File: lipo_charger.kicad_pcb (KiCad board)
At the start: 2 copper layers, 42 x 51 mm, 13 parts, among them P1 CONN_01X02, P2 CONN_01X02, Q1 BC557, Q2 BC547, U1 MCP73831

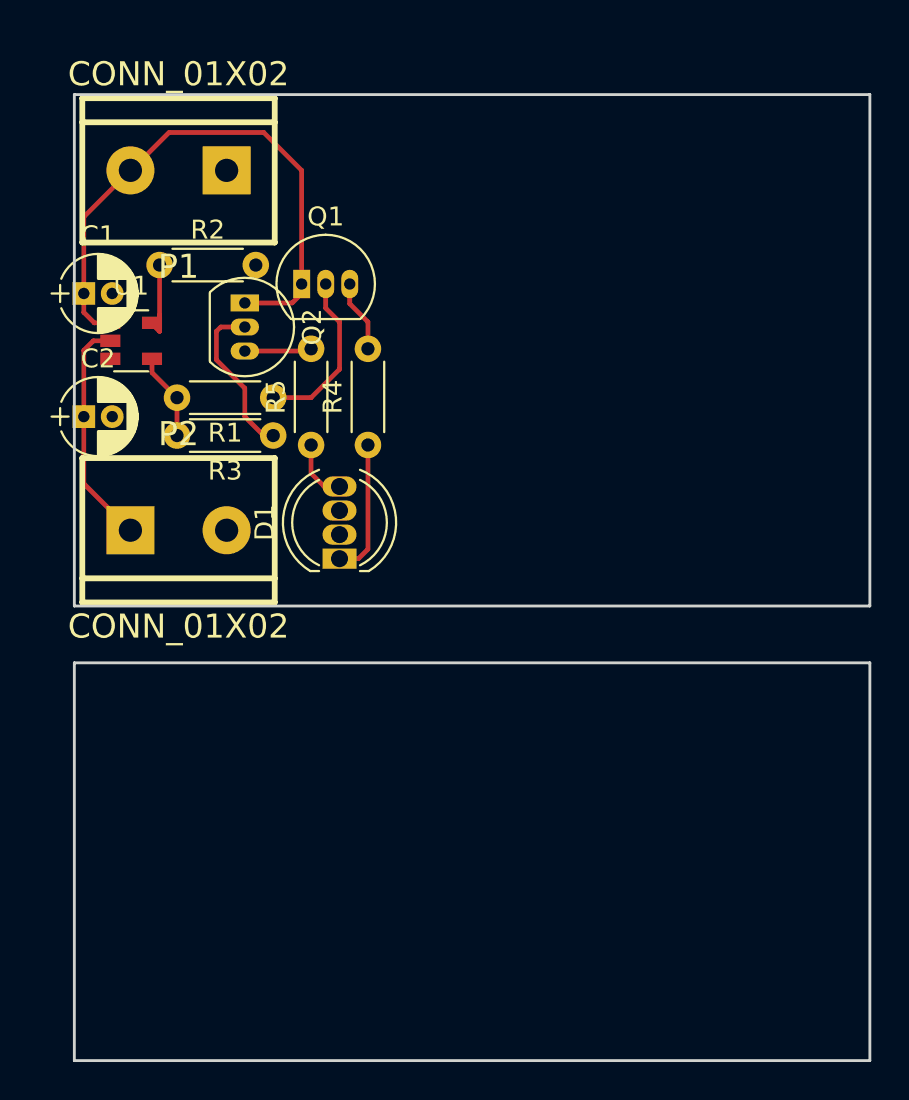
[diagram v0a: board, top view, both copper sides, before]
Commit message: 3x lipo charger with tracks
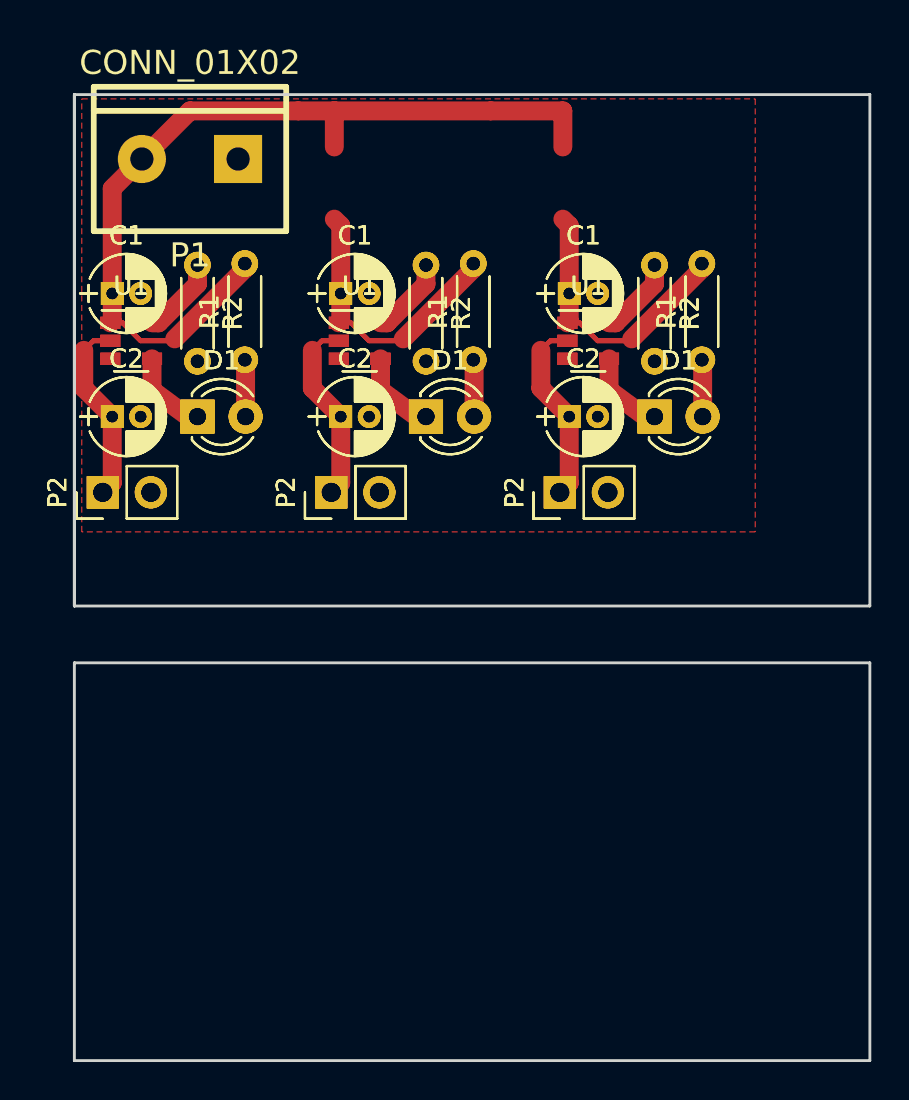
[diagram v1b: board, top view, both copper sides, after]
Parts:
- removed the D1 at (86.0, 46.5)
- removed the P2 at (77.5, 45.0)
- removed Q1: BC557, TO_SOT_Packages_THT:TO-92_Inline_Narrow_Oval
- removed Q2: BC547, TO_SOT_Packages_THT:TO-92_Inline_Narrow_Oval
- removed R3: 2k, Resistors_ThroughHole:R_Axial_DIN0204_L3.6mm_D1.6mm_P5.08mm_Horizontal
- removed R4, R5: 220R, Resistors_ThroughHole:R_Axial_DIN0204_L3.6mm_D1.6mm_P5.08mm_Horizontal
- added C1 (x2): 4.7uF, Capacitors_THT:CP_Radial_D4.0mm_P1.50mm, F.Cu at (98.1, 32.5)
- added C1 (x2): 4.7uF, Capacitors_THT:CP_Radial_D4.0mm_P1.50mm, F.Cu at (86.1, 32.5)
- added C1: 4.7uF, Capacitors_THT:CP_Radial_D4.0mm_P1.50mm, F.Cu at (74.0, 32.5)
- added C2 (x2): 4.7uF, Capacitors_THT:CP_Radial_D4.0mm_P1.50mm, F.Cu at (98.1, 39.0)
- added C2 (x2): 4.7uF, Capacitors_THT:CP_Radial_D4.0mm_P1.50mm, F.Cu at (86.1, 39.0)
- added C2: 4.7uF, Capacitors_THT:CP_Radial_D4.0mm_P1.50mm, F.Cu at (74.0, 39.0)
- added D1 (x2): LED, LEDs:LED_D3.0mm, F.Cu at (102.6, 39.0)
- added D1 (x2): LED, LEDs:LED_D3.0mm, F.Cu at (90.6, 39.0)
- added D1 (x2): LED, LEDs:LED_D3.0mm, F.Cu at (78.5, 39.0)
- added P2 (x2): CONN_01X02, Pin_Headers:Pin_Header_Straight_1x02_Pitch2.54mm, F.Cu at (97.6, 43.0)
- added P2 (x2): CONN_01X02, Pin_Headers:Pin_Header_Straight_1x02_Pitch2.54mm, F.Cu at (85.6, 43.0)
- added P2 (x2): CONN_01X02, Pin_Headers:Pin_Header_Straight_1x02_Pitch2.54mm, F.Cu at (73.5, 43.0)
- added R1 (x2): 220R, Resistors_ThroughHole:R_Axial_DIN0204_L3.6mm_D1.6mm_P5.08mm_Horizontal, F.Cu at (105.1, 36.0)
- added R1 (x2): 220R, Resistors_ThroughHole:R_Axial_DIN0204_L3.6mm_D1.6mm_P5.08mm_Horizontal, F.Cu at (93.1, 36.0)
- added R1: 220R, Resistors_ThroughHole:R_Axial_DIN0204_L3.6mm_D1.6mm_P5.08mm_Horizontal, F.Cu at (81.0, 36.0)
- added R2 (x2): 10k, Resistors_ThroughHole:R_Axial_DIN0204_L3.6mm_D1.6mm_P5.08mm_Horizontal, F.Cu at (102.6, 31.0)
- added R2 (x2): 10k, Resistors_ThroughHole:R_Axial_DIN0204_L3.6mm_D1.6mm_P5.08mm_Horizontal, F.Cu at (90.6, 31.0)
- added R2: 10k, Resistors_ThroughHole:R_Axial_DIN0204_L3.6mm_D1.6mm_P5.08mm_Horizontal, F.Cu at (78.5, 31.0)
- added U1 (x2): MCP73831, TO_SOT_Packages_SMD:SOT-23-5, F.Cu at (99.1, 35.0)
- added U1 (x2): MCP73831, TO_SOT_Packages_SMD:SOT-23-5, F.Cu at (87.1, 35.0)
- added U1: MCP73831, TO_SOT_Packages_SMD:SOT-23-5, F.Cu at (75.0, 35.0)
- R1: value 2k -> 220R
- moved R1 2.50 mm to (81.0, 36.0), turned to 90 degrees
- moved R2 2.00 mm to (78.5, 31.0), turned to 270 degrees
- moved C1 1.50 mm to (74.0, 32.5)
- moved C2 1.50 mm to (74.0, 39.0)
- moved P1 0.85 mm to (78.1, 25.4)
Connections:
- R1 pad 2: /stat -> +5V
- U1 pad 4: /stat -> Net-(D1-Pad1)
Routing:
- net +5V: track 30.6 -> 135.9 mm
- net Net-(C2-Pad1): track 13.5 -> 51.2 mm
- net Net-(D1-Pad1): track 7.21 -> 27.1 mm
- net Net-(D1-Pad2): track 8.92 -> 27.1 mm
- net Net-(R2-Pad1): track 4.12 -> 16.9 mm
- net Net-(Q2-Pad2): track 9.13 -> 0.00 mm
- net /stat: track 4.60 -> 0.00 mm
- net Net-(Q1-Pad3): track 3.82 -> 0.00 mm
- net Net-(Q2-Pad3): track 3.55 -> 0.00 mm
- net Net-(D1-Pad4): track 3.29 -> 0.00 mm
- added copper zone on F.Cu, net GND
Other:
- net class Default: clearance 0.2 -> 0.1; trace_width 0.25 -> 1
- rule trace_clearance: 0.2 -> 0.1
